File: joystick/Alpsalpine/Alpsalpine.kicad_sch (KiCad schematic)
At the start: 1 part

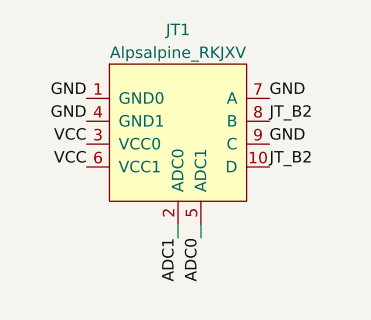
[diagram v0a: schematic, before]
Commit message: update joystick label to global
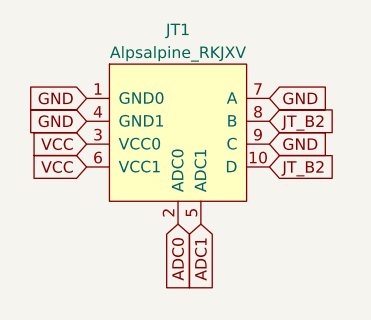
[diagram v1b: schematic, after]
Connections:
- net ADC0: now also JT1.2 (ADC0); no longer JT1.5 (ADC1)
- net ADC1: now also JT1.5 (ADC1); no longer JT1.2 (ADC0)
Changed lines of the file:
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@@
 	(generator_version "9.0")
 	(paper "A4")
-	(wire
-		(pts
-			(xy 113.03 88.9) (xy 113.03 90.424)
-		)
-		(stroke
-			(width 0)
-			(type default)
-		)
-	)
-	(wire
-		(pts
-			(xy 110.49 88.9) (xy 110.49 90.424)
-		)
-		(stroke
-			(width 0)
-			(type default)
-		)
-	)
-	(label "GND"
+	(global_label "ADC1"
+		(shape input)
+		(at 113.03 88.9 270)
+		(fields_autoplaced yes)
+		(effects
+			(font
+				(size 1.27 1.27)
+			)
+			(justify right)
+		)
+		(property "Intersheetrefs" "${INTERSHEET_REFS}"
+			(at 113.03 96.7233 90)
+			(effects
+				(font
+					(size 1.27 1.27)
+				)
+				(justify right)
+				(hide yes)
+			)
+		)
+	)
+	(global_label "GND"
+		(shape input)
+		(at 120.65 74.93 0)
+		(fields_autoplaced yes)
+		(effects
+			(font
+				(size 1.27 1.27)
+			)
+			(justify left)
+		)
+		(property "Intersheetrefs" "${INTERSHEET_REFS}"
+			(at 127.5057 74.93 0)
+			(effects
+				(font
+					(size 1.27 1.27)
+				)
+				(justify left)
+				(hide yes)
+			)
+		)
+	)
+	(global_label "VCC"
+		(shape input)
+		(at 100.33 80.01 180)
+		(fields_autoplaced yes)
+		(effects
+			(font
+				(size 1.27 1.27)
+			)
+			(justify right)
+		)
+		(property "Intersheetrefs" "${INTERSHEET_REFS}"
+			(at 93.7162 80.01 0)
+			(effects
+				(font
+					(size 1.27 1.27)
+				)
+				(justify right)
+				(hide yes)
+			)
+		)
+	)
+	(global_label "VCC"
+		(shape input)
+		(at 100.33 82.55 180)
+		(fields_autoplaced yes)
+		(effects
+			(font
+				(size 1.27 1.27)
+			)
+			(justify right)
+		)
+		(property "Intersheetrefs" "${INTERSHEET_REFS}"
+			(at 93.7162 82.55 0)
+			(effects
+				(font
+					(size 1.27 1.27)
+				)
+				(justify right)
+				(hide yes)
+			)
+		)
+	)
+	(global_label "GND"
+		(shape input)
+		(at 120.65 80.01 0)
+		(fields_autoplaced yes)
+		(effects
+			(font
+				(size 1.27 1.27)
+			)
+			(justify left)
+		)
+		(property "Intersheetrefs" "${INTERSHEET_REFS}"
+			(at 127.5057 80.01 0)
+			(effects
+				(font
+					(size 1.27 1.27)
+				)
+				(justify left)
+				(hide yes)
+			)
+		)
+	)
+	(global_label "GND"
+		(shape input)
 		(at 100.33 74.93 180)
-		(effects
-			(font
-				(size 1.27 1.27)
-			)
-			(justify right bottom)
-		)
-	)
-	(label "GND"
-		(at 120.65 80.01 0)
-		(effects
-			(font
-				(size 1.27 1.27)
-			)
-			(justify left bottom)
-		)
-	)
-	(label "VCC"
-		(at 100.33 80.01 180)
-		(effects
-			(font
-				(size 1.27 1.27)
-			)
-			(justify right bottom)
-		)
-	)
-	(label "JT_B2"
+		(fields_autoplaced yes)
+		(effects
+			(font
+				(size 1.27 1.27)
+			)
+			(justify right)
+		)
+		(property "Intersheetrefs" "${INTERSHEET_REFS}"
+			(at 93.4743 74.93 0)
+			(effects
+				(font
+					(size 1.27 1.27)
+				)
+				(justify right)
+				(hide yes)
+			)
+		)
+	)
+	(global_label "JT_B2"
+		(shape input)
+		(at 120.65 82.55 0)
+		(fields_autoplaced yes)
+		(effects
+			(font
+				(size 1.27 1.27)
+			)
+			(justify left)
+		)
+		(property "Intersheetrefs" "${INTERSHEET_REFS}"
+			(at 129.0175 82.55 0)
+			(effects
+				(font
+					(size 1.27 1.27)
+				)
+				(justify left)
+				(hide yes)
+			)
+		)
+	)
+	(global_label "JT_B2"
+		(shape input)
 		(at 120.65 77.47 0)
-		(effects
-			(font
-				(size 1.27 1.27)
-			)
-			(justify left bottom)
-		)
-	)
-	(label "ADC1"
-		(at 110.49 90.424 270)
-		(effects
-			(font
-				(size 1.27 1.27)
-			)
-			(justify right bottom)
-		)
-	)
-	(label "VCC"
-		(at 100.33 82.55 180)
-		(effects
-			(font
-				(size 1.27 1.27)
-			)
-			(justify right bottom)
-		)
-	)
-	(label "JT_B2"
-		(at 120.65 82.55 0)
-		(effects
-			(font
-				(size 1.27 1.27)
-			)
-			(justify left bottom)
-		)
-	)
-	(label "ADC0"
-		(at 113.03 90.424 270)
-		(effects
-			(font
-				(size 1.27 1.27)
-			)
-			(justify right bottom)
-		)
-	)
-	(label "GND"
+		(fields_autoplaced yes)
+		(effects
+			(font
+				(size 1.27 1.27)
+			)
+			(justify left)
+		)
+		(property "Intersheetrefs" "${INTERSHEET_REFS}"
+			(at 129.0175 77.47 0)
+			(effects
+				(font
+					(size 1.27 1.27)
+				)
+				(justify left)
+				(hide yes)
+			)
+		)
+	)
+	(global_label "ADC0"
+		(shape input)
+		(at 110.49 88.9 270)
+		(fields_autoplaced yes)
+		(effects
+			(font
+				(size 1.27 1.27)
+			)
+			(justify right)
+		)
+		(property "Intersheetrefs" "${INTERSHEET_REFS}"
+			(at 110.49 96.7233 90)
+			(effects
+				(font
+					(size 1.27 1.27)
+				)
+				(justify right)
+				(hide yes)
+			)
+		)
+	)
+	(global_label "GND"
+		(shape input)
 		(at 100.33 77.47 180)
-		(effects
-			(font
-				(size 1.27 1.27)
-			)
-			(justify right bottom)
-		)
-	)
-	(label "GND"
-		(at 120.65 74.93 0)
-		(effects
-			(font
-				(size 1.27 1.27)
-			)
-			(justify left bottom)
-		)
-	)
+		(fields_autoplaced yes)
+		(effects
+			(font
+				(size 1.27 1.27)
+			)
+			(justify right)
+		)
+		(property "Intersheetrefs" "${INTERSHEET_REFS}"
+			(at 93.4743 77.47 0)
+			(effects
+				(font
+					(size 1.27 1.27)
+				)
+				(justify right)
+				(hide yes)
+			)
+		)
+	)

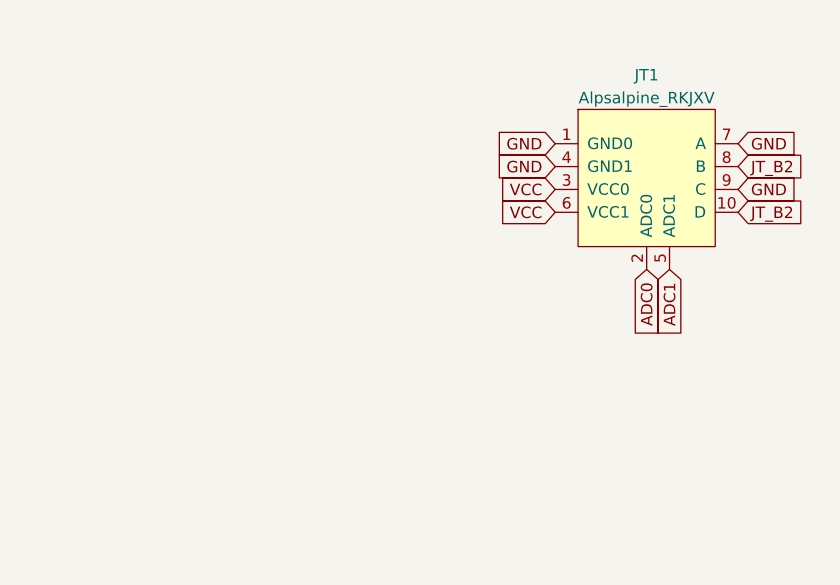
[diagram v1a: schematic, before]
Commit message: add joystick module
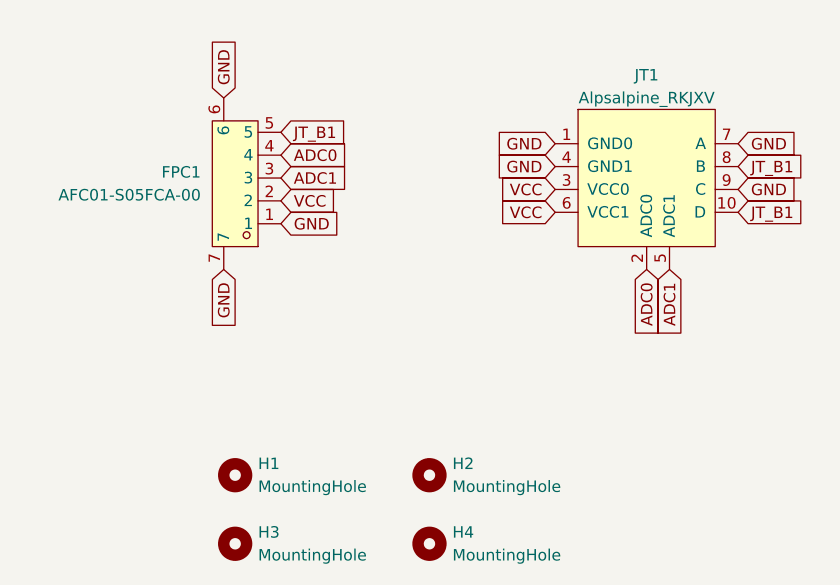
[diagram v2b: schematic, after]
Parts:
- added FPC1: AFC01-S05FCA-00, ErgoCai.pretty:FPC-SMD_AFC01-S05FCA-00, symbol ErgoCai:AFC01-S05FCA-00
- added H1, H2, H3, H4: MountingHole, MountingHole:MountingHole_2.2mm_M2_DIN965, symbol Mechanical:MountingHole
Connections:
- net ADC0: now also FPC1.4
- net ADC1: now also FPC1.3
- net GND: now also FPC1.1, FPC1.6, FPC1.7
- net VCC: now also FPC1.2
- net JT_B2 renamed JT_B1
- net JT_B1: now also FPC1.5

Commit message: update joystick FPC to 6 pins
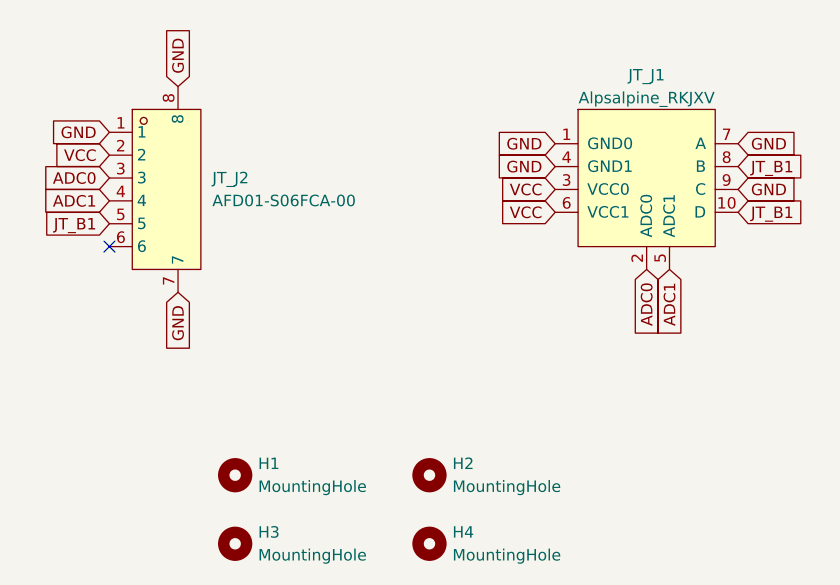
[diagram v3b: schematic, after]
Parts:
- removed FPC1: AFC01-S05FCA-00, ErgoCai.pretty:FPC-SMD_AFC01-S05FCA-00, symbol ErgoCai:AFC01-S05FCA-00
- added JT_J2: AFD01-S06FCA-00, ErgoCai.pretty:FPC-SMD_6P-P0.50_JS_AFD01-S06FCA-00, symbol ErgoCai:AFD01-S06FCA-00
- renumbered JT1 to JT_J1
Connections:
- net ADC0: now also JT_J2.3
- net ADC1: now also JT_J2.4
- net GND: now also JT_J2.1, JT_J2.7, JT_J2.8
- net JT_B1: now also JT_J2.5
- net VCC: now also JT_J2.2
- no-connect marks 0 -> 1
